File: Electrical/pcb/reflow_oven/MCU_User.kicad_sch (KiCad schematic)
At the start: 15 parts, among them J2 Conn_01x06, U3 STM32F030CCTx, Y1 8MHz 8pF

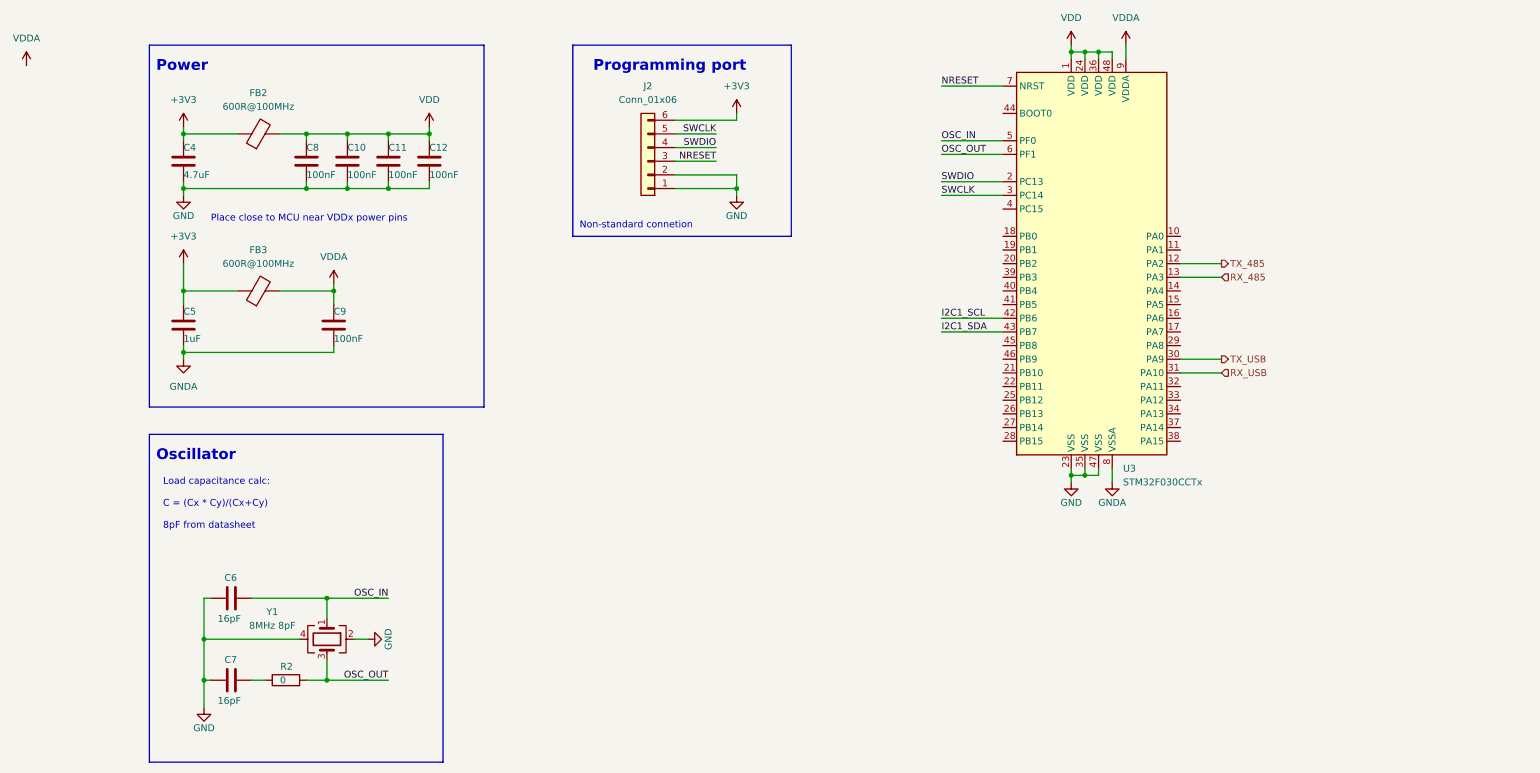
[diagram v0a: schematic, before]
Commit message: interface
partial interface schematic
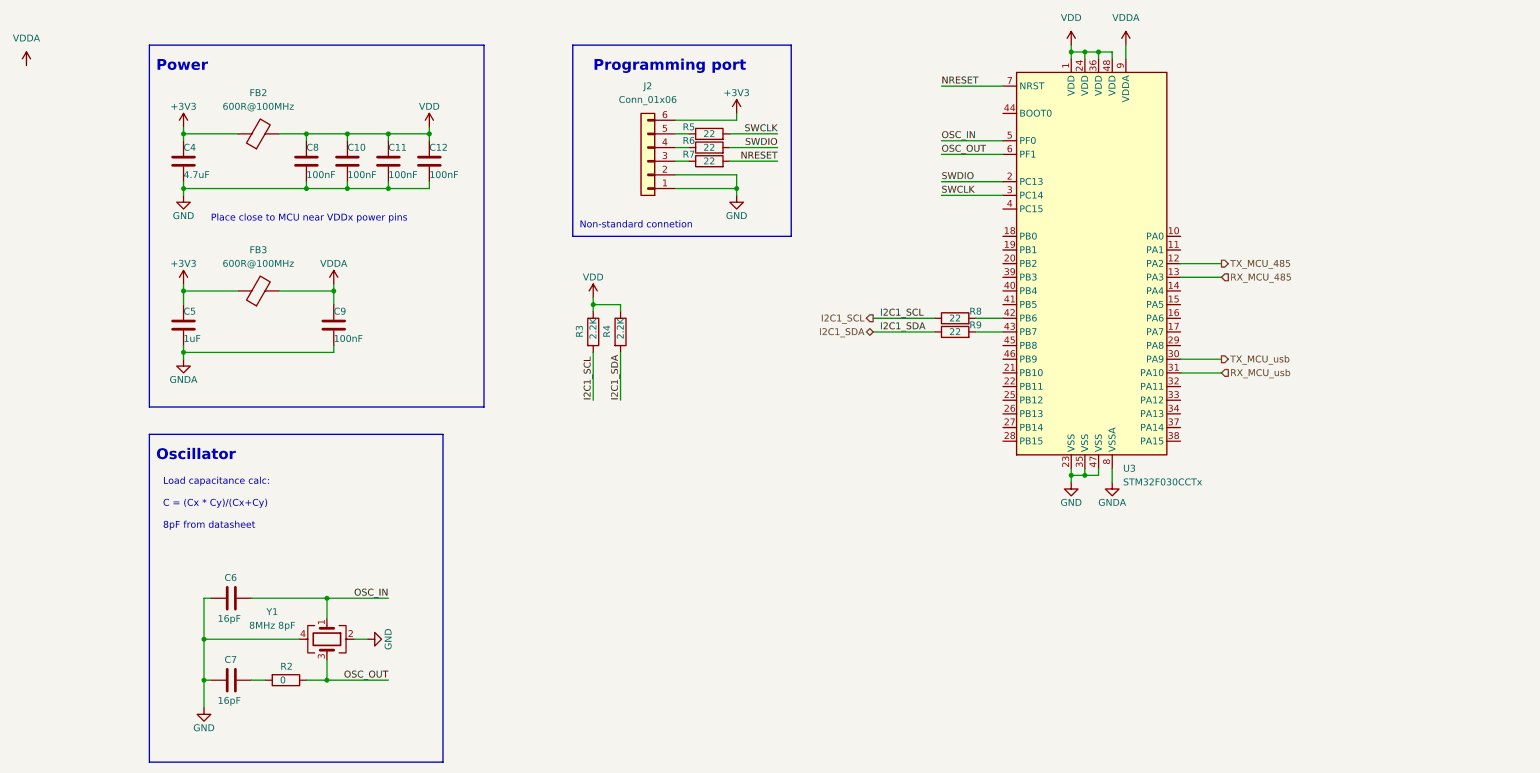
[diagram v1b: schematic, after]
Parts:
- added R3, R4: 2.2K, Resistor_SMD:R_0603_1608Metric, symbol Device:R
- added R5, R6, R7, R8, R9: 22, Resistor_SMD:R_0603_1608Metric, symbol Device:R
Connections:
- net I2C1_SCL: now also R3.2, R8.1; no longer U3.42 (PB6)
- net I2C1_SDA: now also R4.2, R9.1; no longer U3.43 (PB7)
- net NRESET: now also R7.2; no longer J2.3 (Pin_3)
- net SWCLK: now also R5.2; no longer J2.5 (Pin_5)
- net SWDIO: now also R6.2; no longer J2.4 (Pin_4)
- net VDD: now also R3.1, R4.1
- net RX_485 renamed RX_MCU_485
- net RX_USB renamed RX_MCU_usb
- net TX_485 renamed TX_MCU_485
- net TX_USB renamed TX_MCU_usb
- new net: J2.3 (Pin_3), R7.1
- new net: R8.2, U3.42 (PB6)
- new net: R9.2, U3.43 (PB7)
- new net: J2.4 (Pin_4), R6.1
- new net: J2.5 (Pin_5), R5.1

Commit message: analog Sensing
-voltage and current sensor
-zero crossing
-temperature
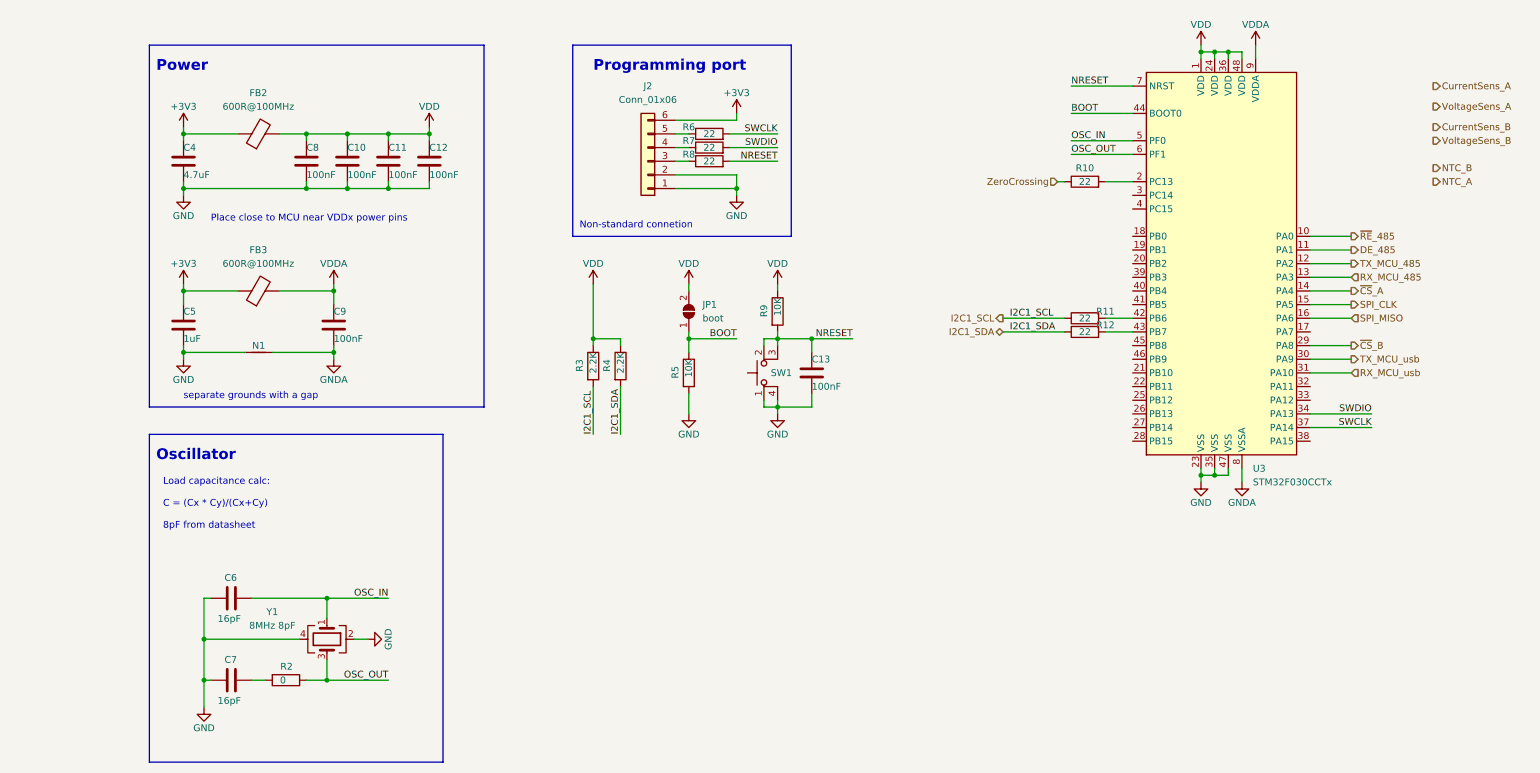
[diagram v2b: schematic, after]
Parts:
- added C13: 100nF, Capacitor_SMD:C_0603_1608Metric, symbol Device:C
- added JP1: boot, Jumper:SolderJumper-2_P1.3mm_Open_RoundedPad1.0x1.5mm, symbol Jumper:SolderJumper_2_Open
- added N1: Net-Tie_2, NetTie:NetTie-2_SMD_Pad2.0mm, symbol CellsBoard-rescue:Net-Tie_2-Device
- added R10: 22, Resistor_SMD:R_0603_1608Metric, symbol Device:R
- added R5, R9: 10K, Resistor_SMD:R_0603_1608Metric, symbol Device:R
- added SW1: SW_MEC_5E, footprint_lib:KMR621NGLFS, symbol Switch:SW_MEC_5E
- renumbered R8 to R11, R9 to R12, R5 to R6, R6 to R7, R7 to R8
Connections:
- net GND: now also C5.2, C13.2, N1.1, R5.2, SW1.1, SW1.4
- net GNDA: now also N1.2; no longer C5.2
- net NRESET: now also C13.1, R9.2, SW1.2, SW1.3 (K)
- net SWCLK: now also U3.37 (PA14); no longer U3.3 (PC14)
- net SWDIO: now also U3.34 (PA13); no longer U3.2 (PC13)
- net VDD: now also JP1.2 (B), R9.1
- net ~{RE}_485: now reaches U3.10 (PA0)
- net DE_485: now reaches U3.11 (PA1)
- net ~{CS}_A: now reaches U3.14 (PA4)
- net SPI_CLK: now reaches U3.15 (PA5)
- net SPI_MISO: now reaches U3.16 (PA6)
- net ~{CS}_B: now reaches U3.29 (PA8)
- net BOOT: now reaches U3.44 (BOOT0)
- net BOOT: now also JP1.1 (A), R5.1
- new net: R10.2, U3.2 (PC13)
- new net ZeroCrossing: R10.1
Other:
- note added: "separate grounds with a gap"
- moved on the sheet: R11, R12, R3, R4, U3

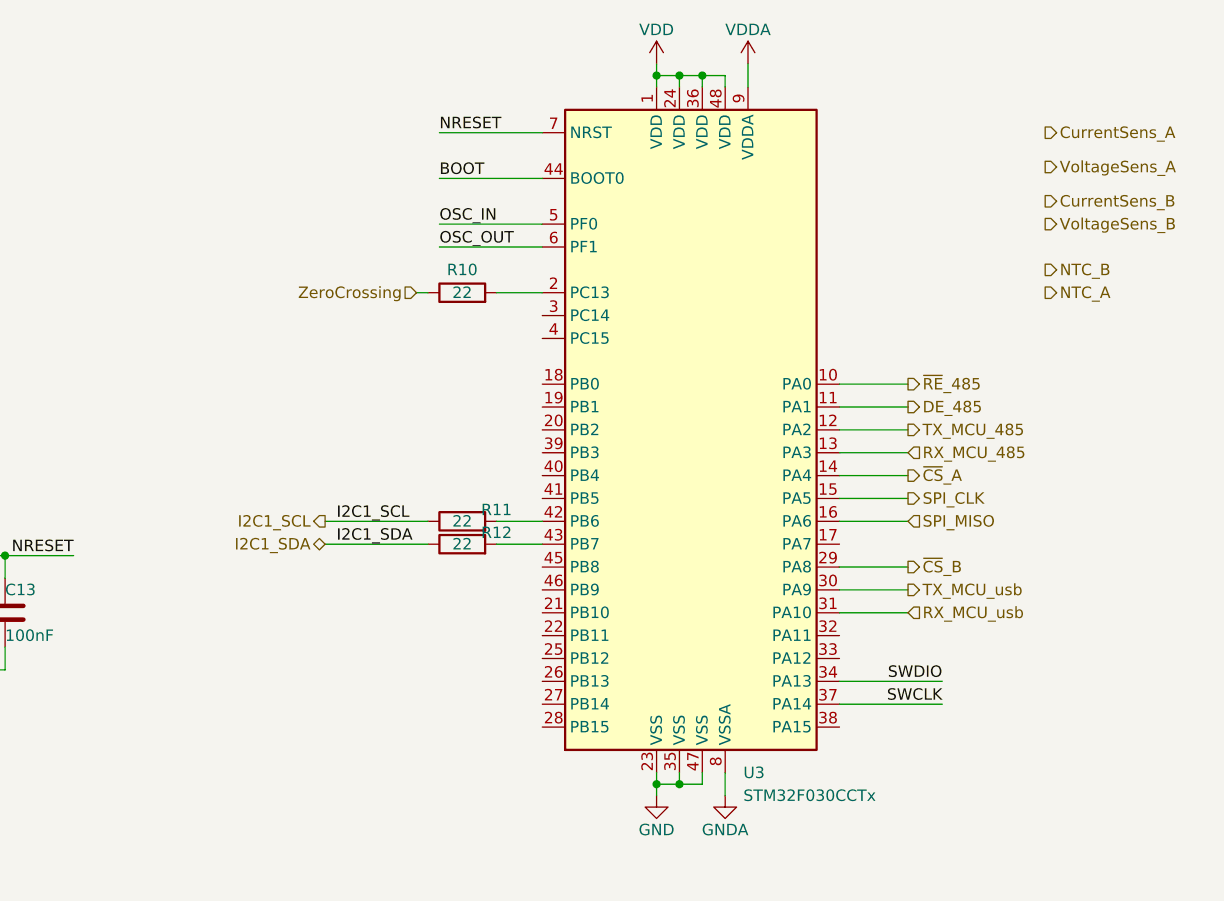
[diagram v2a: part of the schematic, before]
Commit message: schematic
-interface
-micro
todo
output
routing
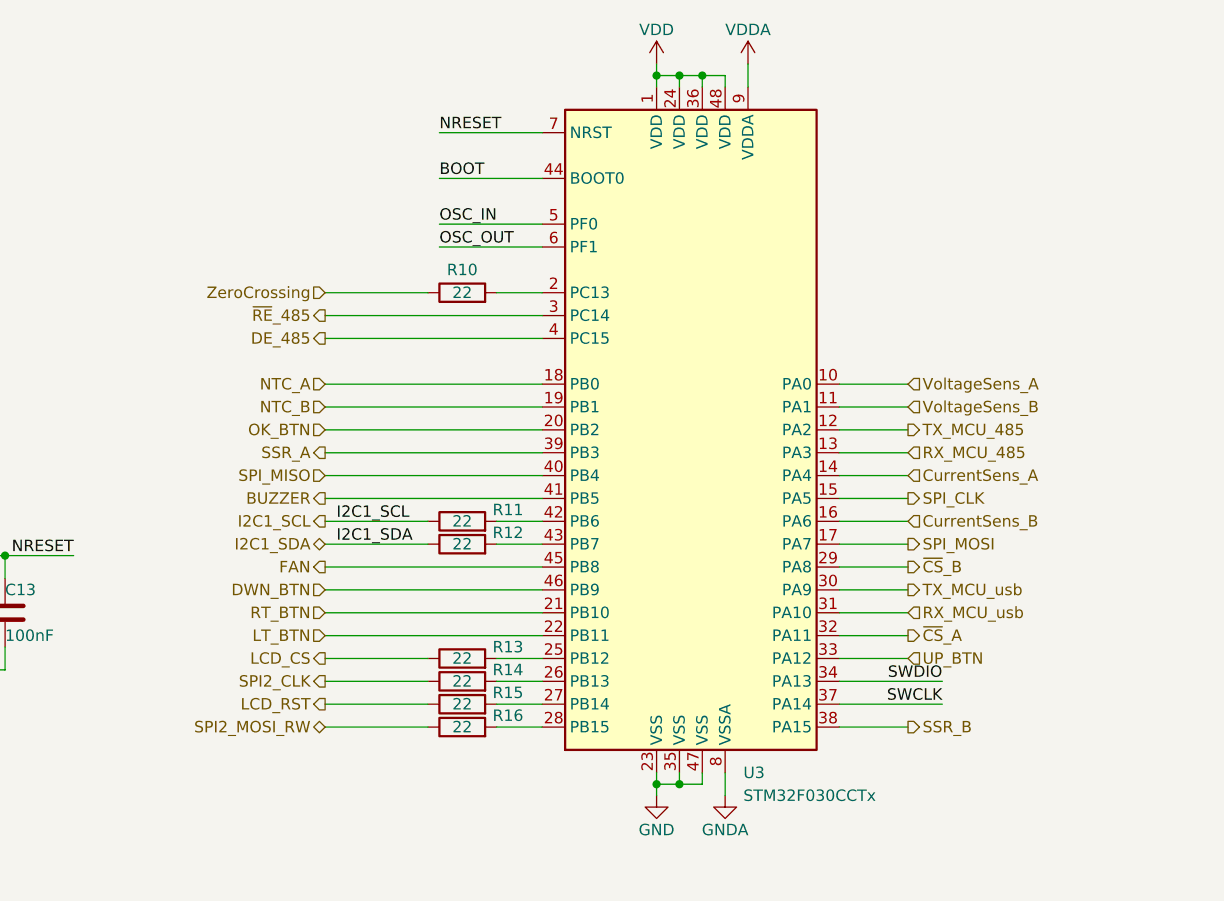
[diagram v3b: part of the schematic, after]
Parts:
- added R13, R14, R15, R16: 22, Resistor_SMD:R_0603_1608Metric, symbol Device:R
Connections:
- net CurrentSens_A: now also U3.14 (PA4)
- net CurrentSens_B: now also U3.16 (PA6)
- net DE_485: now also U3.4 (PC15); no longer U3.11 (PA1)
- net NTC_A: now also U3.18 (PB0)
- net NTC_B: now also U3.19 (PB1)
- net SPI_MISO: now also U3.40 (PB4); no longer U3.16 (PA6)
- net VoltageSens_A: now also U3.10 (PA0)
- net VoltageSens_B: now also U3.11 (PA1)
- net ~{CS}_A: now also U3.32 (PA11); no longer U3.14 (PA4)
- net ~{RE}_485: now also U3.3 (PC14); no longer U3.10 (PA0)
- net SPI_MOSI: now reaches U3.17 (PA7)
- net OK_BTN: now reaches U3.20 (PB2)
- net RT_BTN: now reaches U3.21 (PB10)
- net LT_BTN: now reaches U3.22 (PB11)
- net at U3.25 (PB12): now also R13.2
- net at U3.26 (PB13): now also R14.2
- net at U3.27 (PB14): now also R15.2
- net at U3.28 (PB15): now also R16.2
- net UP_BTN: now reaches U3.33 (PA12)
- net SSR_B: now reaches U3.38 (PA15)
- net SSR_A: now reaches U3.39 (PB3)
- net BUZZER: now reaches U3.41 (PB5)
- net FAN: now reaches U3.45 (PB8)
- net DWN_BTN: now reaches U3.46 (PB9)
- new net LCD_CS: R13.1
- new net LCD_RST: R15.1
- new net SPI2_CLK: R14.1
- new net SPI2_MOSI_RW: R16.1
